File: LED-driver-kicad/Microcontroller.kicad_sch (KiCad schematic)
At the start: 12 parts, among them J2 Conn_01x02_Socket, J3 Conn_01x05_Socket, SW1 SW_SPDT, U6 PIC16F18026-ISL, U9 25AA02E64T-I/OT

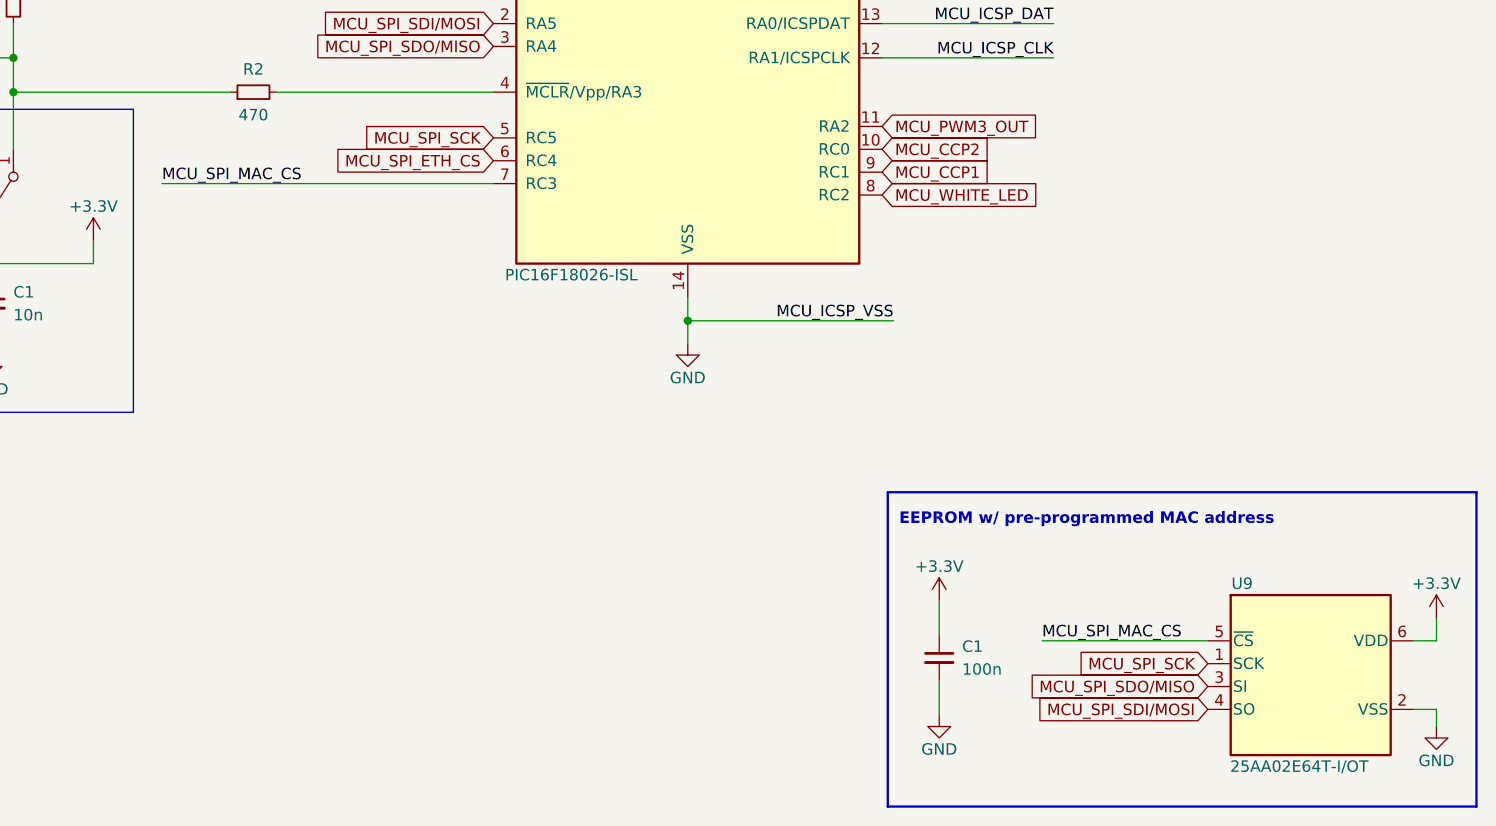
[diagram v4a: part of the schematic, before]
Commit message: remove EEPROM MAC address IC
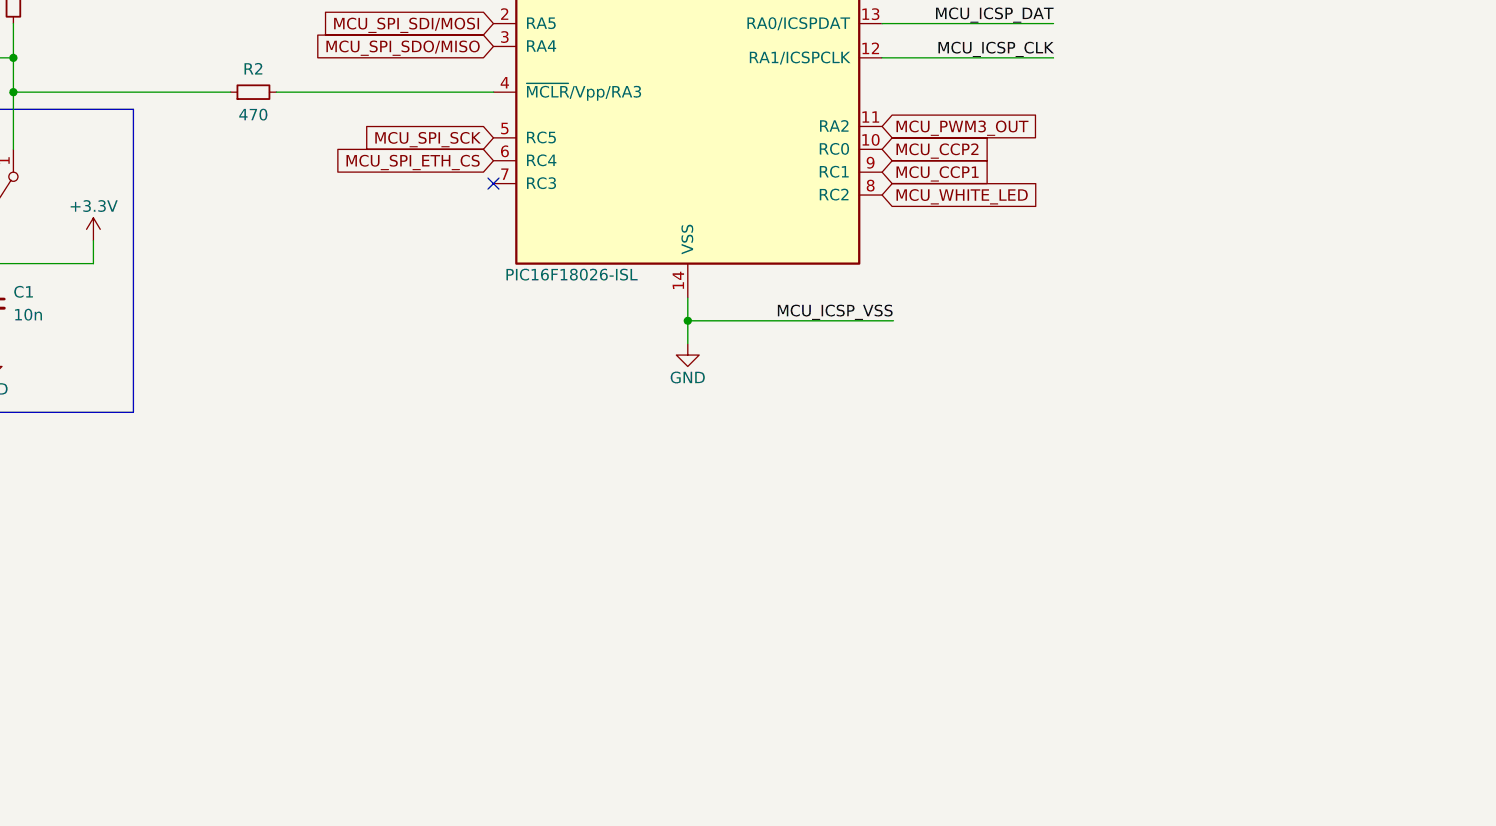
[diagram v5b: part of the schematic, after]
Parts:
- removed C1: 100n, symbol Device:C_Small
- removed U9: 25AA02E64T-I/OT, Mahabeer_Package_SOT_SMD:SOT-23-6_MC_MCH-Memory_Microchip_25AA02E64T-IOT, symbol Memory_Microchip_25AA02E64T-IOT:25AA02E64T-I_OT
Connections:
- net MCU_SPI_MAC_CS: no longer names the net of U6.7 (RC3)
- no-connect marks 0 -> 1
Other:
- note removed: "EEPROM w/ pre-programmed MAC address"
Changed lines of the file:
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@@
   (junction (at 154.94 107.95) (diameter 0) (color 0 0 0 0)
   )
+  (no_connect (at 133.35 92.71))
   (wire (pts (xy 154.94 105.41) (xy 154.94 107.95))
     (stroke (width 0) (type default))
@@
     (stroke (width 0) (type default))
   )
-  (wire (pts (xy 238.125 143.51) (xy 238.125 140.97))
-    (stroke (width 0) (type default))
-  )
   (wire (pts (xy 42.545 39.37) (xy 20.955 39.37))
     (stroke (width 0) (type default))
@@
     (stroke (width 0) (type default))
   )
-  (wire (pts (xy 238.125 151.13) (xy 235.585 151.13))
-    (stroke (width 0) (type default))
-  )
-  (wire (pts (xy 194.31 143.51) (xy 212.725 143.51))
-    (stroke (width 0) (type default))
-  )
   (wire (pts (xy 77.47 101.6) (xy 77.47 103.505))
     (stroke (width 0) (type default))
   )
-  (wire (pts (xy 235.585 143.51) (xy 238.125 143.51))
-    (stroke (width 0) (type default))
-  )
   (wire (pts (xy 176.53 74.93) (xy 195.58 74.93))
     (stroke (width 0) (type default))
@@
     (stroke (width 0) (type default))
   )
-  (wire (pts (xy 238.125 153.035) (xy 238.125 151.13))
-    (stroke (width 0) (type default))
-  )
   (wire (pts (xy 154.94 52.705) (xy 154.94 55.245))
     (stroke (width 0) (type default))
   )
-  (wire (pts (xy 96.52 92.71) (xy 133.35 92.71))
-    (stroke (width 0) (type default))
-  )
   (wire (pts (xy 80.01 78.74) (xy 80.01 82.55))
     (stroke (width 0) (type default))
@@
     (stroke (width 0) (type default))
   )
-  (wire (pts (xy 182.88 147.955) (xy 182.88 151.765))
-    (stroke (width 0) (type default))
-  )
   (wire (pts (xy 61.595 86.995) (xy 61.595 91.44))
-    (stroke (width 0) (type default))
-  )
-  (wire (pts (xy 182.88 139.065) (xy 182.88 142.875))
     (stroke (width 0) (type default))
   )
@@
     (fill (type none))
   )
-  (rectangle (start 177.165 127) (end 242.57 161.925)
-    (stroke (width 0.254) (type default))
-    (fill (type none))
-  )
   (text "In Circuit Serial Programming (ICSP)" (at 20.955 22.86 0)
-    (effects (font (size 1.27 1.27) (thickness 0.254) bold) (justify left bottom))
-  )
-  (text "EEPROM w/ pre-programmed MAC address" (at 178.435 130.81 0)
     (effects (font (size 1.27 1.27) (thickness 0.254) bold) (justify left bottom))
   )
@@
     (effects (font (size 1.27 1.27)) (justify left bottom))
   )
-  (label "MCU_SPI_MAC_CS" (at 96.52 92.71 0) (fields_autoplaced)
-    (effects (font (size 1.27 1.27)) (justify left bottom))
-  )
   (label "MCU_ICSP_MCLR" (at 20.955 31.75 0) (fields_autoplaced)
-    (effects (font (size 1.27 1.27)) (justify left bottom))
-  )
-  (label "MCU_SPI_MAC_CS" (at 194.31 143.51 0) (fields_autoplaced)
     (effects (font (size 1.27 1.27)) (justify left bottom))
   )
@@
     (effects (font (size 1.27 1.27)) (justify left bottom))
   )
-  (global_label "MCU_SPI_SDI{slash}MOSI" (shape input) (at 212.725 151.13 180) (fields_autoplaced)
-    (effects (font (size 1.27 1.27)) (justify right))
-    (property "Intersheetrefs" "${INTERSHEET_REFS}" (at 191.6574 151.13 0)
-      (effects (font (size 1.27 1.27)) (justify right) hide)
-    )
-  )
   (global_label "MCU_CCP2" (shape input) (at 176.53 88.9 0) (fields_autoplaced)
     (effects (font (size 1.27 1.27)) (justify left))
     (property "Intersheetrefs" "${INTERSHEET_REFS}" (at 189.5542 88.9 0)
       (effects (font (size 1.27 1.27)) (justify left) hide)
-    )
-  )
-  (global_label "MCU_SPI_SDO{slash}MISO" (shape input) (at 212.725 148.59 180) (fields_autoplaced)
-    (effects (font (size 1.27 1.27)) (justify right))
-    (property "Intersheetrefs" "${INTERSHEET_REFS}" (at 190.9317 148.59 0)
-      (effects (font (size 1.27 1.27)) (justify right) hide)
     )
   )
@@
     )
   )
-  (global_label "MCU_SPI_SCK" (shape input) (at 212.725 146.05 180) (fields_autoplaced)
-    (effects (font (size 1.27 1.27)) (justify right))
-    (property "Intersheetrefs" "${INTERSHEET_REFS}" (at 196.9189 146.05 0)
-      (effects (font (size 1.27 1.27)) (justify right) hide)
-    )
-  )
   (global_label "MCU_PWM5_OUT" (shape input) (at 60.96 39.37 0) (fields_autoplaced)
     (effects (font (size 1.27 1.27)) (justify left))
     (property "Intersheetrefs" "${INTERSHEET_REFS}" (at 78.9432 39.37 0)
       (effects (font (size 1.27 1.27)) (justify left) hide)
-    )
-  )
-  (symbol (lib_id "power:+3.3V") (at 182.88 139.065 0) (unit 1)
-    (in_bom yes) (on_board yes) (dnp no)
-    (property "Reference" "#PWR037" (at 182.88 142.875 0)
-      (effects (font (size 1.27 1.27)) hide)
-    )
-    (property "Value" "+3.3V" (at 182.88 135.255 0)
-      (effects (font (size 1.27 1.27)))
-    )
-    (property "Footprint" "" (at 182.88 139.065 0)
-      (effects (font (size 1.27 1.27)) hide)
-    )
-    (property "Datasheet" "" (at 182.88 139.065 0)
-      (effects (font (size 1.27 1.27)) hide)
-    )
-    (pin "1")
-    (instances
-      (project "LED-driver-kicad"
-        (path "/2b071084-2ab6-4896-84cc-45b211479417/9127cd83-cae7-424d-ad3b-8a9e0439da28"
-          (reference "#PWR037") (unit 1)
-        )
-      )
-    )
-  )
-  (symbol (lib_id "Device:C_Small") (at 182.88 145.415 0) (unit 1)
-    (in_bom yes) (on_board yes) (dnp no) (fields_autoplaced)
-    (property "Reference" "C1" (at 185.42 144.1513 0)
-      (effects (font (size 1.27 1.27)) (justify left))
-    )
-    (property "Value" "100n" (at 185.42 146.6913 0)
-      (effects (font (size 1.27 1.27)) (justify left))
-    )
-    (property "Footprint" "" (at 182.88 145.415 0)
-      (effects (font (size 1.27 1.27)) hide)
-    )
-    (property "Datasheet" "~" (at 182.88 145.415 0)
-      (effects (font (size 1.27 1.27)) hide)
-    )
-    (pin "1")
-    (pin "2")
-    (instances
-      (project "LED-driver-kicad"
-        (path "/2b071084-2ab6-4896-84cc-45b211479417"
-          (reference "C1") (unit 1)
-        )
-        (path "/2b071084-2ab6-4896-84cc-45b211479417/9127cd83-cae7-424d-ad3b-8a9e0439da28"
-          (reference "C31") (unit 1)
-        )
-      )
-    )
-  )
-  (symbol (lib_id "power:GND") (at 238.125 153.035 0) (unit 1)
-    (in_bom yes) (on_board yes) (dnp no)
-    (property "Reference" "#PWR04" (at 238.125 159.385 0)
-      (effects (font (size 1.27 1.27)) hide)
-    )
-    (property "Value" "GND" (at 238.125 156.845 0)
-      (effects (font (size 1.27 1.27)))
-    )
-    (property "Footprint" "" (at 238.125 153.035 0)
-      (effects (font (size 1.27 1.27)) hide)
-    )
-    (property "Datasheet" "" (at 238.125 153.035 0)
-      (effects (font (size 1.27 1.27)) hide)
-    )
-    (pin "1")
-    (instances
-      (project "LED-driver-kicad"
-        (path "/2b071084-2ab6-4896-84cc-45b211479417"
-          (reference "#PWR04") (unit 1)
-        )
-        (path "/2b071084-2ab6-4896-84cc-45b211479417/9127cd83-cae7-424d-ad3b-8a9e0439da28"
-          (reference "#PWR04") (unit 1)
-        )
-      )
     )
   )
@@
     )
   )
-  (symbol (lib_id "power:+3.3V") (at 238.125 140.97 0) (unit 1)
-    (in_bom yes) (on_board yes) (dnp no)
-    (property "Reference" "#PWR05" (at 238.125 144.78 0)
-      (effects (font (size 1.27 1.27)) hide)
-    )
-    (property "Value" "+3.3V" (at 238.125 137.16 0)
-      (effects (font (size 1.27 1.27)))
-    )
-    (property "Footprint" "" (at 238.125 140.97 0)
-      (effects (font (size 1.27 1.27)) hide)
-    )
-    (property "Datasheet" "" (at 238.125 140.97 0)
-      (effects (font (size 1.27 1.27)) hide)
-    )
-    (pin "1")
-    (instances
-      (project "LED-driver-kicad"
-        (path "/2b071084-2ab6-4896-84cc-45b211479417"
-          (reference "#PWR05") (unit 1)
-        )
-        (path "/2b071084-2ab6-4896-84cc-45b211479417/9127cd83-cae7-424d-ad3b-8a9e0439da28"
-          (reference "#PWR05") (unit 1)
-        )
-      )
-    )
-  )
   (symbol (lib_id "Device:R_Small") (at 80.01 72.39 0) (unit 1)
     (in_bom yes) (on_board yes) (dnp no)
@@
     )
   )
-  (symbol (lib_id "Memory_Microchip_25AA02E64T-IOT:25AA02E64T-I_OT") (at 224.155 147.32 0) (unit 1)
-    (in_bom yes) (on_board yes) (dnp no)
-    (property "Reference" "U9" (at 216.535 137.16 0)
-      (effects (font (size 1.27 1.27)))
-    )
-    (property "Value" "25AA02E64T-I/OT" (at 222.885 157.48 0)
-      (effects (font (size 1.27 1.27)))
-    )
-    (property "Footprint" "Mahabeer_Package_SOT_SMD:SOT-23-6_MC_MCH-Memory_Microchip_25AA02E64T-IOT" (at 224.155 160.02 0)
-      (effects (font (size 1.27 1.27) italic) hide)
-    )
-    (property "Datasheet" "25AA02E64T-I/OT" (at 224.155 157.48 0)
-      (effects (font (size 1.27 1.27) italic) hide)
-    )
-    (pin "1")
-    (pin "2")
-    (pin "3")
-    (pin "4")
-    (pin "5")
-    (pin "6")
-    (instances
-      (project "LED-driver-kicad"
-        (path "/2b071084-2ab6-4896-84cc-45b211479417/9127cd83-cae7-424d-ad3b-8a9e0439da28"
-          (reference "U9") (unit 1)
-        )
-      )
-    )
-  )
   (symbol (lib_id "Device:LED_Small_Filled") (at 61.595 93.98 270) (mirror x) (unit 1)
     (in_bom yes) (on_board yes) (dnp no)
@@
         )
       )
-    )
-  )
-  (symbol (lib_id "power:GND") (at 182.88 151.765 0) (unit 1)
-    (in_bom yes) (on_board yes) (dnp no)
-    (property "Reference" "#PWR038" (at 182.88 158.115 0)
-      (effects (font (size 1.27 1.27)) hide)
-    )
-    (property "Value" "GND" (at 182.88 155.575 0)
-      (effects (font (size 1.27 1.27)))
-    )
-    (property "Footprint" "" (at 182.88 151.765 0)
-      (effects (font (size 1.27 1.27)) hide)
-    )
-    (property "Datasheet" "" (at 182.88 151.765 0)
-      (effects (font (size 1.27 1.27)) hide)
-    )
-    (pin "1")
-    (instances
-      (project "LED-driver-kicad"
-        (path "/2b071084-2ab6-4896-84cc-45b211479417/9127cd83-cae7-424d-ad3b-8a9e0439da28"
-          (reference "#PWR038") (unit 1)
-        )
-      )

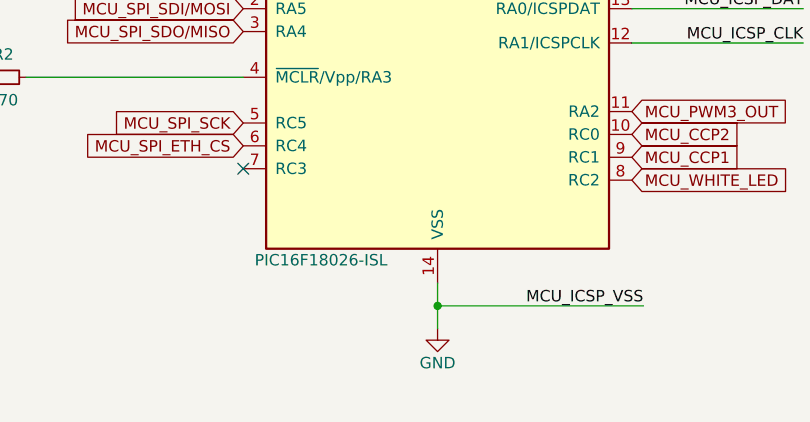
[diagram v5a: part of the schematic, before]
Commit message: connect unused IO to pull down resistor
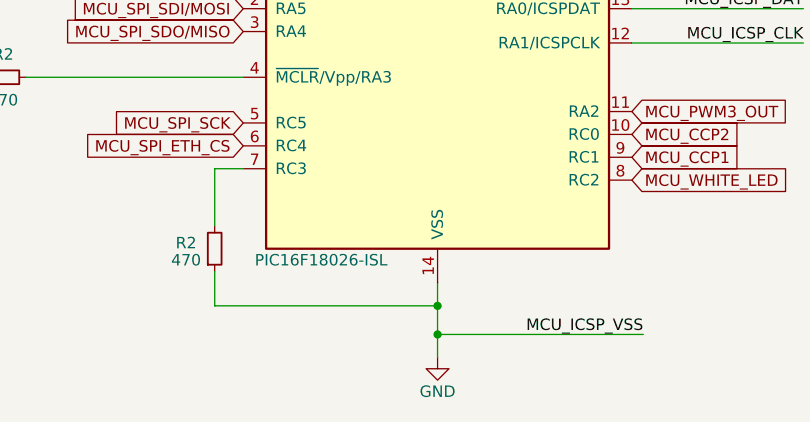
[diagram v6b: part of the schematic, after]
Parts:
- added R2: 470, symbol Device:R_Small
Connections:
- net GND: now also R2.1
- net at U6.7 (RC3): now also R2.2
- no-connect marks 1 -> 0
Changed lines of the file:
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@@
   (junction (at 80.01 78.74) (diameter 0) (color 0 0 0 0)
   )
+  (junction (at 154.94 107.95) (diameter 0) (color 0 0 0 0)
+  )
   (junction (at 80.01 82.55) (diameter 0) (color 0 0 0 0)
   )
@@
   (junction (at 77.47 109.855) (diameter 0) (color 0 0 0 0)
   )
-  (junction (at 154.94 107.95) (diameter 0) (color 0 0 0 0)
-  )
-  (no_connect (at 133.35 92.71))
+  (junction (at 154.94 111.125) (diameter 0) (color 0 0 0 0)
+  )
   (wire (pts (xy 154.94 105.41) (xy 154.94 107.95))
     (stroke (width 0) (type default))
   )
+  (wire (pts (xy 130.175 107.95) (xy 154.94 107.95))
+    (stroke (width 0) (type default))
+  )
   (wire (pts (xy 154.94 60.96) (xy 154.94 62.23))
     (stroke (width 0) (type default))
@@
     (stroke (width 0) (type default))
   )
-  (wire (pts (xy 154.94 107.95) (xy 154.94 110.49))
-    (stroke (width 0) (type default))
-  )
   (wire (pts (xy 154.94 55.245) (xy 123.825 55.245))
     (stroke (width 0) (type default))
@@
     (stroke (width 0) (type default))
   )
-  (wire (pts (xy 154.94 107.95) (xy 177.8 107.95))
+  (wire (pts (xy 154.94 111.125) (xy 177.8 111.125))
     (stroke (width 0) (type default))
   )
@@
     (stroke (width 0) (type default))
   )
+  (wire (pts (xy 130.175 104.14) (xy 130.175 107.95))
+    (stroke (width 0) (type default))
+  )
   (wire (pts (xy 42.545 41.91) (xy 20.955 41.91))
     (stroke (width 0) (type default))
   )
+  (wire (pts (xy 154.94 111.125) (xy 154.94 113.665))
+    (stroke (width 0) (type default))
+  )
   (wire (pts (xy 61.595 96.52) (xy 61.595 99.06))
     (stroke (width 0) (type default))
@@
     (stroke (width 0) (type default))
   )
+  (wire (pts (xy 154.94 107.95) (xy 154.94 111.125))
+    (stroke (width 0) (type default))
+  )
   (wire (pts (xy 61.595 104.14) (xy 61.595 109.855))
     (stroke (width 0) (type default))
@@
     (stroke (width 0) (type default))
   )
+  (wire (pts (xy 133.35 92.71) (xy 130.175 92.71))
+    (stroke (width 0) (type default))
+  )
   (wire (pts (xy 123.825 55.245) (xy 123.825 59.055))
     (stroke (width 0) (type default))
@@
   )
   (wire (pts (xy 61.595 86.995) (xy 61.595 91.44))
+    (stroke (width 0) (type default))
+  )
+  (wire (pts (xy 130.175 92.71) (xy 130.175 99.06))
     (stroke (width 0) (type default))
   )
@@
     (effects (font (size 1.27 1.27)) (justify left bottom))
   )
-  (label "MCU_ICSP_VSS" (at 177.8 107.95 180) (fields_autoplaced)
+  (label "MCU_ICSP_VSS" (at 177.8 111.125 180) (fields_autoplaced)
     (effects (font (size 1.27 1.27)) (justify right bottom))
   )
@@
     )
   )
-  (symbol (lib_id "power:GND") (at 154.94 110.49 0) (unit 1)
-    (in_bom yes) (on_board yes) (dnp no)
-    (property "Reference" "#PWR039" (at 154.94 116.84 0)
-      (effects (font (size 1.27 1.27)) hide)
-    )
-    (property "Value" "GND" (at 154.94 114.3 0)
-      (effects (font (size 1.27 1.27)))
-    )
-    (property "Footprint" "" (at 154.94 110.49 0)
-      (effects (font (size 1.27 1.27)) hide)
-    )
-    (property "Datasheet" "" (at 154.94 110.49 0)
+  (symbol (lib_id "power:GND") (at 154.94 113.665 0) (unit 1)
+    (in_bom yes) (on_board yes) (dnp no)
+    (property "Reference" "#PWR039" (at 154.94 120.015 0)
+      (effects (font (size 1.27 1.27)) hide)
+    )
+    (property "Value" "GND" (at 154.94 117.475 0)
+      (effects (font (size 1.27 1.27)))
+    )
+    (property "Footprint" "" (at 154.94 113.665 0)
+      (effects (font (size 1.27 1.27)) hide)
+    )
+    (property "Datasheet" "" (at 154.94 113.665 0)
       (effects (font (size 1.27 1.27)) hide)
     )
@@
         )
       )
+    )
+  )
+  (symbol (lib_id "Device:R_Small") (at 130.175 101.6 0) (mirror x) (unit 1)
+    (in_bom yes) (on_board yes) (dnp no)
+    (property "Reference" "R2" (at 127 100.965 0)
+      (effects (font (size 1.27 1.27)))
+    )
+    (property "Value" "470" (at 127 102.87 0)
+      (effects (font (size 1.27 1.27)))
+    )
+    (property "Footprint" "" (at 130.175 101.6 0)
+      (effects (font (size 1.27 1.27)) hide)
+    )
+    (property "Datasheet" "~" (at 130.175 101.6 0)
+      (effects (font (size 1.27 1.27)) hide)
+    )
+    (pin "1")
+    (pin "2")
+    (instances
+      (project "LED-driver-kicad"
+        (path "/2b071084-2ab6-4896-84cc-45b211479417"
+          (reference "R2") (unit 1)
+        )
+        (path "/2b071084-2ab6-4896-84cc-45b211479417/9127cd83-cae7-424d-ad3b-8a9e0439da28"
+          (reference "R40") (unit 1)
+        )
+      )

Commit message: update comments and title blocks
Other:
- title: (none) -> Photogrammetry Rig - LED Driver
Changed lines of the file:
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@@
 (kicad_sch (version 20230121) (generator eeschema)
   (paper "A4")
+  (title_block
+    (title "Photogrammetry Rig - LED Driver")
+    (date "2023-08-02")
+    (rev "0.1.0")
+  )
   (junction (at 154.94 55.245) (diameter 0) (color 0 0 0 0)
   )
